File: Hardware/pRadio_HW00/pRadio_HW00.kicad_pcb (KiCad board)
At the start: 2 copper layers, 30 x 71 mm, 10 parts, among them J1 PSoM_ESP32S2_Carrier_Board, J2 USB4510-03-1-A, J3 SJ2-3514A-SMT-TR, J4 S2B-PH-SM4-TB, SW1 450405020524, SW2 SW_Push, SW3 ACZ11BR1E-15FA1-20C, SW4 ACZ11BR1E-15FA1-20C, U1 SA818S

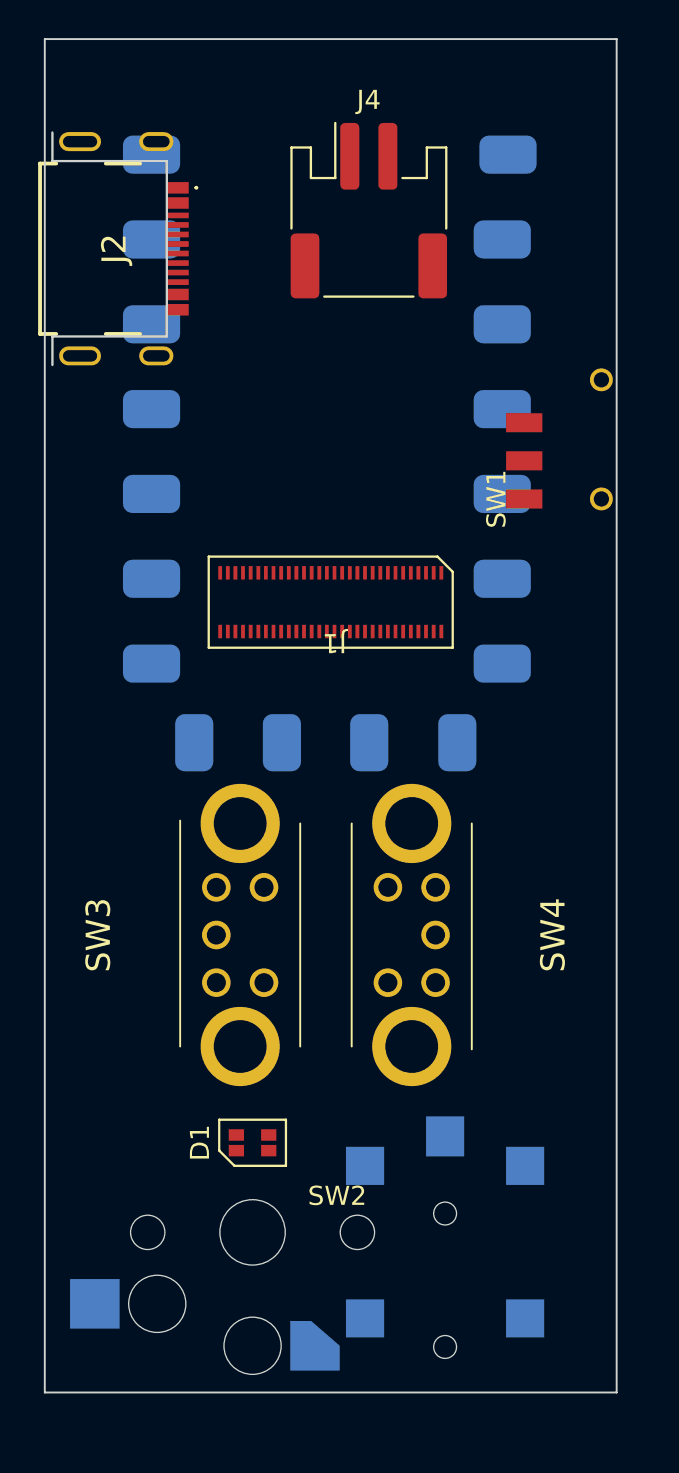
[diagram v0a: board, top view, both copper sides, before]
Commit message: Working on layout to see how compact it can get
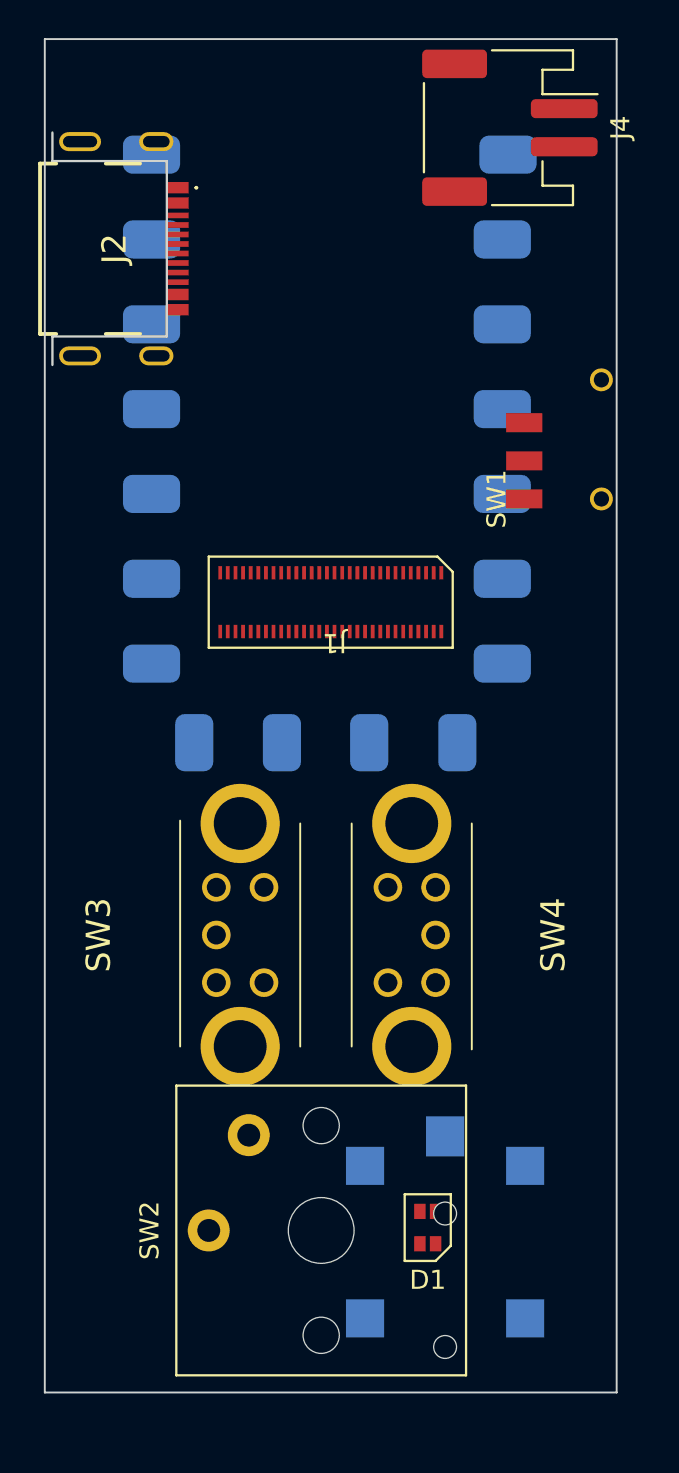
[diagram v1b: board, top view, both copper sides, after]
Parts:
- SW2: footprint Component_lib:Kailh_socket_PG1350 -> Component_lib:SW_Kailh_Choc_V1
- moved D1 10.2 mm to (110.1, 118.3), turned to 90 degrees
- moved J4 8.58 mm to (114.4, 60.6), turned to -90 degrees
- moved SW2 3.60 mm to (104.5, 118.5), turned to 90 degrees

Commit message: Schematic done
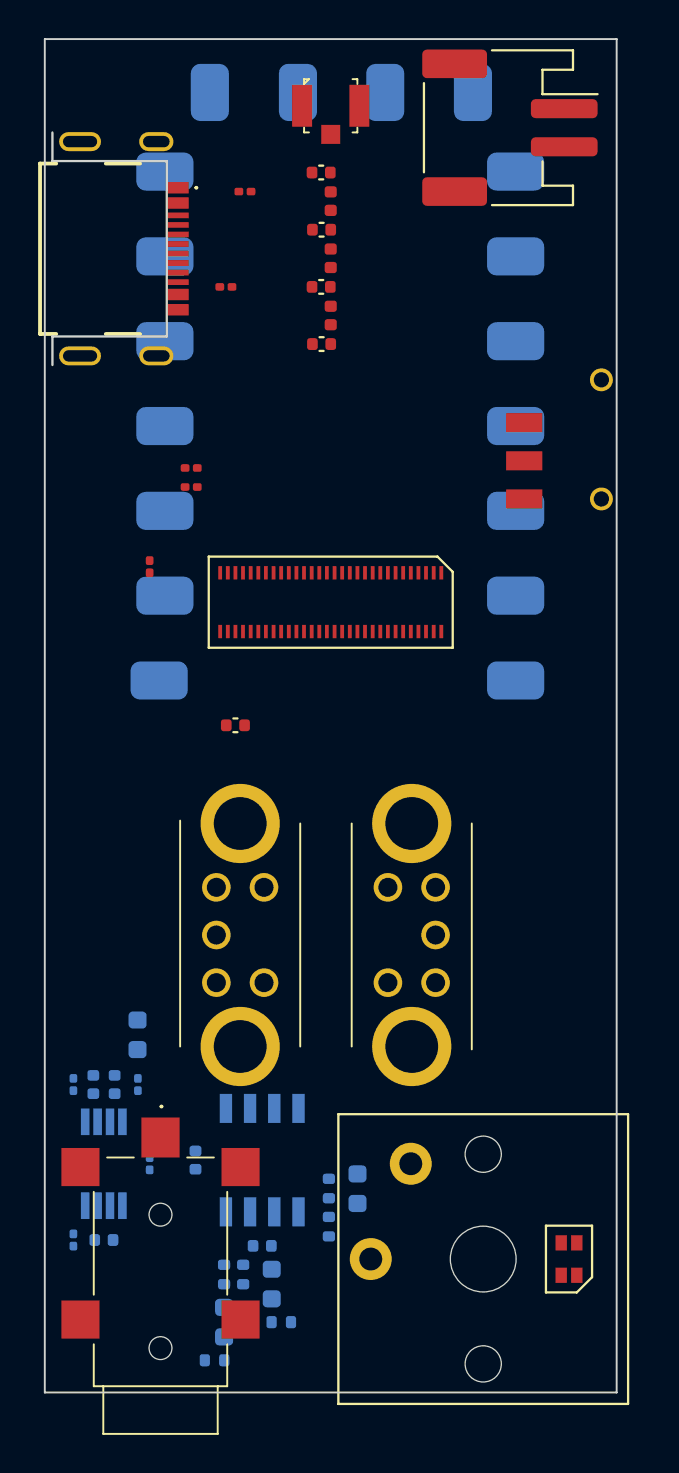
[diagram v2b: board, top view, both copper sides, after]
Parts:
- removed U1: SA818S, Component_lib:RF818
- added C400: 100n, Capacitor_SMD:C_0402_1005Metric, F.Cu at (100.0, 92.0)
- added C401: 20p, Capacitor_SMD:C_0402_1005Metric, F.Cu at (104.5, 72.0)
- added C402: 36p, Capacitor_SMD:C_0402_1005Metric, F.Cu at (104.5, 69.0)
- added C403: 36p, Capacitor_SMD:C_0402_1005Metric, F.Cu at (104.5, 66.0)
- added C404: 20p, Capacitor_SMD:C_0402_1005Metric, F.Cu at (104.5, 63.0)
- added C500: 390n, Capacitor_SMD:C_0603_1608Metric, B.Cu at (94.9, 108.2)
- added C501: 10p, Capacitor_SMD:C_0402_1005Metric, B.Cu at (93.7, 110.8)
- added C502: 100n, Capacitor_SMD:C_0402_1005Metric, B.Cu at (92.5, 110.8)
- added C503: 100n, Capacitor_SMD:C_0402_1005Metric, B.Cu at (93.1, 119.0)
- added C600: 2u2, Capacitor_SMD:C_0603_1608Metric, B.Cu at (106.4, 116.3)
- added C601: 4u7, Capacitor_SMD:C_0603_1608Metric, B.Cu at (101.9, 121.3)
- added C602: 10p, Capacitor_SMD:C_0402_1005Metric, B.Cu at (101.4, 119.3)
- added C603: 2u2, Capacitor_SMD:C_0603_1608Metric, B.Cu at (99.4, 123.3)
- added C604: 100n, Capacitor_SMD:C_0402_1005Metric, B.Cu at (97.9, 114.8)
- added IC500: LM4871MMX_NOPB, Component_lib:SOP65P490X110-8N, B.Cu at (93.1, 115.0)
- added IC600: LM358D, Component_lib:SOIC127P600X175-8N, B.Cu at (101.4, 114.8)
- added J400: U.FL-R-SMT-1_40_, Component_lib:u.fl, F.Cu at (105.0, 59.5)
- added L400: 56n, Inductor_SMD:L_0402_1005Metric, F.Cu at (105.0, 70.5)
- added L401: 68n, Inductor_SMD:L_0402_1005Metric, F.Cu at (105.0, 67.5)
- added L402: 56n, Inductor_SMD:L_0402_1005Metric, F.Cu at (105.0, 64.5)
- added R100: 5k1, Resistor_SMD:R_0201_0603Metric, F.Cu at (100.5, 64.0)
- added R101: 5k1, Resistor_SMD:R_0201_0603Metric, F.Cu at (99.5, 69.0)
- added R400: 5k1, Resistor_SMD:R_0201_0603Metric, F.Cu at (95.5, 83.7)
- added R401: 0, Resistor_SMD:R_0201_0603Metric, F.Cu at (97.7, 78.5)
- added R402: 0, Resistor_SMD:R_0201_0603Metric, F.Cu at (97.7, 79.5)
- added R500: 20k, Resistor_SMD:R_0201_0603Metric, B.Cu at (95.5, 115.0)
- added R501: 20k, Resistor_SMD:R_0201_0603Metric, B.Cu at (94.9, 110.8)
- added R502: 10k, Resistor_SMD:R_0201_0603Metric, B.Cu at (91.5, 110.8)
- added R503: 0, Resistor_SMD:R_0201_0603Metric, B.Cu at (91.5, 119.0)
- added R600: 100k, Resistor_SMD:R_0402_1005Metric, B.Cu at (104.9, 118.3)
- added R601: 100k, Resistor_SMD:R_0402_1005Metric, B.Cu at (104.9, 116.3)
- added R602: 6k, Resistor_SMD:R_0402_1005Metric, B.Cu at (102.4, 123.3)
- added R603: 10, Resistor_SMD:R_0402_1005Metric, B.Cu at (99.4, 120.8)
- added R604: 100k, Resistor_SMD:R_0402_1005Metric, B.Cu at (98.9, 125.3)
- added R605: 100k, Resistor_SMD:R_0402_1005Metric, B.Cu at (100.4, 120.8)
- added U400: SA868S, Component_lib:RF818, B.Cu at (96.0, 58.5)
- J101: renamed from J3; moved to F.Cu
- moved J101 14.9 mm to (96.1, 121.4)
- moved SW302 8.63 mm to (113.0, 120.0)
- moved D300 7.59 mm to (117.5, 120.0)
- renumbered D1 to D300, J2 to J100, J4 to J102, J1 to J200, SW1 to SW100, SW4 to SW300, SW3 to SW301, SW2 to SW302
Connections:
- D300 pad 1: unconnected-(D1-VSS-Pad1) -> GND
- D300 pad 2: unconnected-(D1-VDD-Pad2) -> /VSYS
- D300 pad 3: unconnected-(D1-DIN-Pad3) -> /LED_DATA
- J100 pad A1: Net-(J2-GND-PadA1) -> GND
- J100 pad A12: Net-(J2-GND-PadA1) -> GND
- J100 pad A4: Net-(J2-VBUS-PadA4) -> VBUS
- J100 pad A5: unconnected-(J2-CC1-PadA5) -> Net-(J100-CC1)
- J100 pad A6: unconnected-(J2-D+-PadA6) -> /D+
- J100 pad A7: unconnected-(J2-D--PadA7) -> /D-
- J100 pad A9: Net-(J2-VBUS-PadA4) -> VBUS
- J100 pad B5: unconnected-(J2-CC2-PadB5) -> Net-(J100-CC2)
- J100 pad B6: unconnected-(J2-D+-PadB6) -> /D+
- J100 pad B7: unconnected-(J2-D--PadB7) -> /D-
- J100 pad MH1: Net-(J2-PadMH1) -> GND
- J100 pad MH2: Net-(J2-PadMH1) -> GND
- J100 pad MH3: Net-(J2-PadMH1) -> GND
- J100 pad MH4: Net-(J2-PadMH1) -> GND
- J101 pad 1: unconnected-(J3-SLEEVE-Pad1) -> GND
- J101 pad 3: unconnected-(J3-RING_1-Pad3) -> /MIC
- J101 pad 4: unconnected-(J3-RING_2-Pad4) -> /SPEAKER
- J101 pad A2: unconnected-(J3-TIP_1-PadA2) -> /EXT_PTT
- J101 pad B2: unconnected-(J3-TIP_2-PadB2) -> /EXT_MIC_DET
- J102 pad 1: unconnected-(J4-Pin_1-Pad1) -> Net-(J102-Pin_1)
- J102 pad 2: unconnected-(J4-Pin_2-Pad2) -> GND
- J102 pad MP: unconnected-(J4-MountPin-PadMP) -> GND
- J200 pad 1: unconnected-(J1-GND-Pad1) -> GND
- J200 pad 10: unconnected-(J1-VBUS-Pad10) -> VBUS
- J200 pad 11: unconnected-(J1-IO5-Pad11) -> /POWERDOWN
- J200 pad 12: unconnected-(J1-VBUS-Pad12) -> VBUS
- J200 pad 13: unconnected-(J1-IO6-Pad13) -> /SQ
- J200 pad 14: unconnected-(J1-VSYS-Pad14) -> /VSYS
- J200 pad 15: unconnected-(J1-IO7-Pad15) -> /L_A
- J200 pad 16: unconnected-(J1-VSYS-Pad16) -> /VSYS
- J200 pad 17: unconnected-(J1-IO8-Pad17) -> /L_B
- J200 pad 18: unconnected-(J1-3V3-Pad18) -> +3V3
- J200 pad 19: unconnected-(J1-IO9-Pad19) -> /L_PB
- J200 pad 2: unconnected-(J1-GND-Pad2) -> GND
- J200 pad 20: unconnected-(J1-3V3-Pad20) -> +3V3
- J200 pad 21: unconnected-(J1-IO10-Pad21) -> /R_A
- J200 pad 22: unconnected-(J1-GND-Pad22) -> GND
- J200 pad 23: unconnected-(J1-IO11-Pad23) -> /R_B
- J200 pad 24: unconnected-(J1-GND-Pad24) -> GND
- J200 pad 25: unconnected-(J1-IO12-Pad25) -> /R_PB
- J200 pad 27: unconnected-(J1-IO13-Pad27) -> /PB_PTT
- J200 pad 29: unconnected-(J1-IO14-Pad29) -> /EXT_MIC_DET
- J200 pad 31: unconnected-(J1-IO15-Pad31) -> /EXT_PTT
- J200 pad 33: unconnected-(J1-IO16-Pad33) -> /PTT
- J200 pad 35: unconnected-(J1-IO17/DAC-Pad35) -> /MIC
- J200 pad 37: unconnected-(J1-IO18/DAC-Pad37) -> /AUDIO_IN
- J200 pad 41: unconnected-(J1-GND-Pad41) -> GND
- J200 pad 54: unconnected-(J1-GND-Pad54) -> GND
- J200 pad 56: unconnected-(J1-D+-Pad56) -> /D+
- J200 pad 58: unconnected-(J1-D--Pad58) -> /D-
- J200 pad 59: unconnected-(J1-GND-Pad59) -> GND
- J200 pad 6: unconnected-(J1-VBAT-Pad6) -> /VBAT
- J200 pad 60: unconnected-(J1-GND-Pad60) -> GND
- J200 pad 7: unconnected-(J1-IO3-Pad7) -> /LED_DATA
- J200 pad 8: unconnected-(J1-VBAT-Pad8) -> /VBAT
- J200 pad 9: unconnected-(J1-IO4-Pad9) -> /TX_POWER
- SW100 pad 1: unconnected-(SW1-A-Pad1) -> /VBAT
- SW100 pad 3: unconnected-(SW1-B-Pad3) -> Net-(J102-Pin_1)
- SW300 pad S1: unconnected-(SW4-PadS1) -> /L_PB
- SW300 pad S2: unconnected-(SW4-PadS2) -> GND
- SW301 pad S1: unconnected-(SW3-PadS1) -> /R_PB
- SW301 pad S2: unconnected-(SW3-PadS2) -> GND
- SW302 pad 1: unconnected-(SW2-Pad1) -> GND
- SW302 pad 2: unconnected-(SW2-Pad2) -> /PB_PTT

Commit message: Working on routing
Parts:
- removed the J100 at (93.0, 67.0)
- removed R100, R101: 5k1, Resistor_SMD:R_0201_0603Metric
- C400: moved to B.Cu
- moved C400 36.1 mm to (110.5, 57.5), turned to 0 degrees
- moved J101 31.5 mm to (97.0, 86.9)
- moved R400 27.3 mm to (117.0, 66.8)
- moved SW100 23.8 mm to (94.4, 70.4), turned to -90 degrees
- moved R402 16.5 mm to (112.8, 72.8), turned to -90 degrees
- moved R401 15.4 mm to (112.0, 72.8), turned to -90 degrees
- moved C401 14.6 mm to (97.0, 59.5), turned to -90 degrees
- moved J200 13.3 mm to (117.4, 80.6), turned to 90 degrees
- moved L400 12.3 mm to (98.5, 60.0), turned to 0 degrees
- moved C402 10.5 mm to (100.0, 59.5), turned to -90 degrees
- moved L401 8.28 mm to (101.5, 60.0), turned to 0 degrees
- moved C403 6.66 mm to (103.0, 59.5), turned to -90 degrees
- moved J400 4.53 mm to (109.5, 60.0), turned to -90 degrees
- moved L402 4.53 mm to (104.5, 60.0), turned to 0 degrees
- moved C404 3.81 mm to (106.0, 59.5), turned to -90 degrees
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- renumbered J101 to J100, J102 to J101
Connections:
- net Net-(J102-Pin_1) renamed /VBAT_IN
- J200 pad 11: /POWERDOWN -> /TX_POWER
- J200 pad 13: /SQ -> /VHF_RX
- J200 pad 15: /L_A -> /VHF_TX
- J200 pad 17: /L_B -> /R_PB
- J200 pad 19: /L_PB -> /R_A
- J200 pad 21: /R_A -> /R_B
- J200 pad 23: /R_B -> /L_PB
- J200 pad 25: /R_PB -> /L_B
- J200 pad 27: /PB_PTT -> /L_A
- J200 pad 29: /EXT_MIC_DET -> /SQ
- J200 pad 31: /EXT_PTT -> unconnected-(J200-IO15-Pad31)
- J200 pad 33: /PTT -> unconnected-(J200-IO16-Pad33)
- J200 pad 35: /MIC -> /AUDIO_IN
- J200 pad 37: /AUDIO_IN -> /MIC
- J200 pad 46: unconnected-(J200-IO40-Pad46) -> /LED_DATA
- J200 pad 5: unconnected-(J200-IO2-Pad5) -> /EXT_PTT
- J200 pad 52: unconnected-(J200-IO42-Pad52) -> /EXT_MIC_DET
- J200 pad 7: /LED_DATA -> /PB_PTT
- J200 pad 9: /TX_POWER -> /POWERDOWN
- SW300 pad MH1: (no net) -> GND
- SW300 pad MH2: (no net) -> GND
- SW301 pad MH1: (no net) -> GND
- SW301 pad MH2: (no net) -> GND
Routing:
- net /MIC_AMPED: track 0.00 -> 37.6 mm
- net /EXT_PTT: track 0.00 -> 33.7 mm
- net /VHF_TX: track 0.00 -> 22.8 mm, vias 0 -> 1
- net /VHF_RX: track 0.00 -> 21.0 mm, vias 0 -> 1
- net /TX_POWER: track 0.00 -> 18.7 mm, vias 0 -> 1
- net /POWERDOWN: track 0.00 -> 16.9 mm, vias 0 -> 1
- net /MIC: track 0.00 -> 9.55 mm, vias 0 -> 1
- net /SPEAKER: track 0.00 -> 6.04 mm, vias 0 -> 1
- net /MIC_AMP_OUT: track 0.00 -> 5.78 mm
- net /PB_PTT: track 0.00 -> 5.02 mm
- net /MIC_AMP_-: track 0.00 -> 4.91 mm
- net +3V3: track 0.00 -> 4.76 mm
- net /VHF_ANT_OUT: track 0.00 -> 4.74 mm, vias 0 -> 1
- net /SPK_AMP_IN: track 0.00 -> 4.44 mm
- net /MIC_AMP_+: track 0.00 -> 4.33 mm
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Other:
- copper layers 2 -> 4
